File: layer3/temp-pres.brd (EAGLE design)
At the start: 16.5 x 12.7 mm, 9 parts, among them U1 TMP1021:1, U2 MS5803-14BA

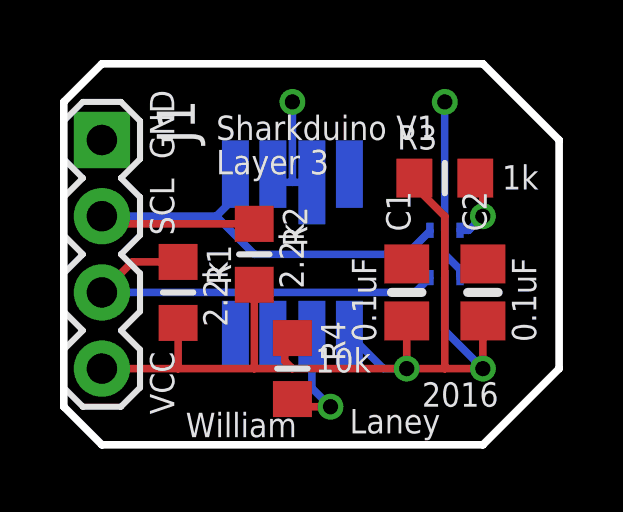
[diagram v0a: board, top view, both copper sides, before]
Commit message: silk screen
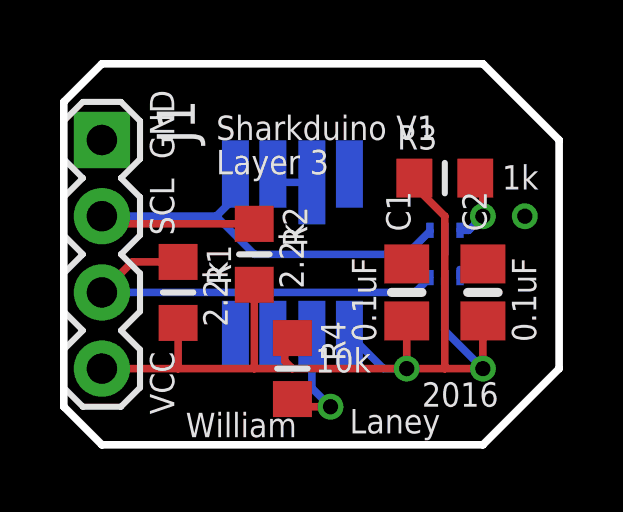
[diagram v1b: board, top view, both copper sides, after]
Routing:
- net GND: track 10.7 -> 3.00 mm, vias 2 -> 1
- added copper zone on layer 16, net GND
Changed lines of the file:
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@@
 <contactref element="C1" pad="2"/>
 <contactref element="C2" pad="2"/>
-<wire x1="8.27" y1="8.75" x2="7.62" y2="8.75" width="0.254" layer="16"/>
-<wire x1="7.62" y1="8.75" x2="7.245" y2="8.75" width="0.254" layer="16"/>
+<wire x1="8.27" y1="8.75" x2="7.245" y2="8.75" width="0.254" layer="16"/>
 <wire x1="7.245" y1="8.75" x2="6.97" y2="9.025" width="0.254" layer="16"/>
 <wire x1="8.27" y1="8.75" x2="8.27" y2="8.24" width="0.254" layer="16"/>
 <wire x1="13.205840625" y1="5.573584375" x2="13.205840625" y2="5.844159375" width="0.254" layer="16"/>
-<wire x1="13.205840625" y1="5.844159375" x2="12.7" y2="6.35" width="0.254" layer="16"/>
 <wire x1="12.7" y1="6.35" x2="12.7" y2="7.146696875" width="0.254" layer="16"/>
 <wire x1="12.7" y1="7.146696875" x2="12.696696875" y2="7.15" width="0.254" layer="16"/>
-<wire x1="12.696696875" y1="7.15" x2="12.696696875" y2="11.426696875" width="0.254" layer="16"/>
-<wire x1="12.696696875" y1="11.426696875" x2="12.7" y2="11.43" width="0.254" layer="16"/>
-<via x="12.7" y="11.43" extent="1-16" drill="0.508"/>
-<via x="7.62" y="11.43" extent="1-16" drill="0.508"/>
-<wire x1="7.62" y1="11.43" x2="7.62" y2="8.75" width="0.254" layer="16"/>
 <polygon width="0.254" layer="1" isolate="0.3048">
 <vertex x="0" y="11.43"/>
@@
 <vertex x="1.27" y="12.7"/>
 </polygon>
+<polygon width="0.254" layer="16" isolate="0.3048">
+<vertex x="1.524" y="12.7"/>
+<vertex x="13.97" y="12.7"/>
+<vertex x="16.51" y="10.16"/>
+<vertex x="16.51" y="2.54"/>
+<vertex x="13.97" y="0"/>
+<vertex x="1.143" y="0"/>
+<vertex x="1.143" y="0.127"/>
+<vertex x="0" y="1.27"/>
+<vertex x="0" y="11.43"/>
+<vertex x="1.27" y="12.7"/>
+</polygon>
+<via x="15.367" y="7.62" extent="1-16" drill="0.508"/>
 </signal>
 <signal name="SCL">

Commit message: tweeaked resistor placement
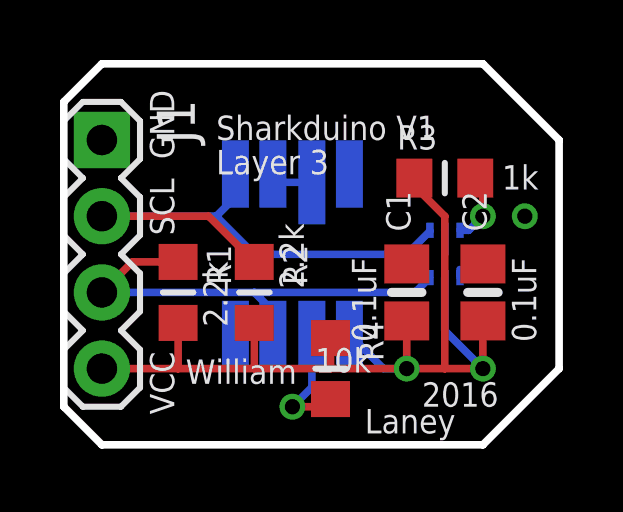
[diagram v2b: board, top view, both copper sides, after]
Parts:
- moved R4 1.27 mm to (8.89, 2.54)
- moved R2 1.27 mm to (6.35, 5.08)
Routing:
- net +3V3: track 34.6 -> 33.0 mm
- net SCL: track 18.7 -> 19.2 mm
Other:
- board text added: "MS5803-14BA"
- board text added: "SDA"
- board text added: "TMP102"
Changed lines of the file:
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@@
 <text x="5.08" y="10.16" size="0.8128" layer="21" font="vector" ratio="15">Sharkduino V1</text>
 <text x="5.08" y="9.017" size="0.8128" layer="21" font="vector" ratio="15">Layer 3</text>
-<text x="4.064" y="0.254" size="0.8128" layer="21" font="vector" ratio="15">William</text>
-<text x="9.525" y="0.381" size="0.8128" layer="21" font="vector" ratio="15">Laney</text>
+<text x="4.064" y="2.032" size="0.8128" layer="21" font="vector" ratio="15">William</text>
+<text x="10.033" y="0.381" size="0.8128" layer="21" font="vector" ratio="15">Laney</text>
 <text x="11.938" y="1.27" size="0.8128" layer="21" font="vector" ratio="15">2016</text>
+<text x="12.7" y="10.16" size="0.8128" layer="22" font="vector" ratio="15" rot="MR0">MS5803-14BA</text>
+<text x="11.049" y="5.207" size="0.8128" layer="22" font="vector" ratio="15" rot="MR180">TMP102</text>
+<text x="2.921" y="9.525" size="0.8128" layer="22" font="vector" ratio="15" rot="MR90">GND</text>
+<text x="2.921" y="6.604" size="0.8128" layer="22" font="vector" ratio="15" rot="MR90">SCL</text>
+<text x="2.921" y="1.27" size="0.8128" layer="22" font="vector" ratio="15" rot="MR90">VCC</text>
+<text x="2.921" y="4.064" size="0.8128" layer="22" font="vector" ratio="15" rot="MR90">SDA</text>
 </plain>
 <attributes>
@@
 </element>
 <element name="R1" library="microbuilder" package="_0805MP" value="2.2K" x="3.81" y="5.08" rot="R270"/>
-<element name="R2" library="microbuilder" package="_0805MP" value="2.2K" x="6.35" y="6.35" rot="R270"/>
+<element name="R2" library="microbuilder" package="_0805MP" value="2.2K" x="6.35" y="5.08" rot="R270"/>
 <element name="R3" library="microbuilder" package="_0805MP" value="1K" x="12.7" y="8.89"/>
-<element name="R4" library="microbuilder" package="_0805MP" value="10K" x="7.62" y="2.54" rot="R270"/>
+<element name="R4" library="microbuilder" package="_0805MP" value="10K" x="8.89" y="2.54" rot="R270"/>
 <element name="U1" library="SparkFun-Sensors" package="SOT563-2" value="TMP1021:1" x="12.7" y="6.35" rot="MR270"/>
 <element name="U2" library="MS5803" package="MS5803" value="MS5803-14BA" x="7.62" y="6.35" rot="MR270">
@@
 <wire x1="5.72" y1="8.26" x2="5.08" y2="7.62" width="0.254" layer="16"/>
 <wire x1="5.08" y1="7.62" x2="1.27" y2="7.62" width="0.254" layer="16"/>
-<wire x1="6.35" y1="7.366" x2="1.524" y2="7.366" width="0.254" layer="1"/>
-<wire x1="1.524" y1="7.366" x2="1.27" y2="7.62" width="0.254" layer="1"/>
 <wire x1="12.20203125" y1="7.15" x2="12.20203125" y2="7.12203125" width="0.254" layer="16"/>
 <wire x1="12.20203125" y1="7.12203125" x2="11.43" y2="6.35" width="0.254" layer="16"/>
 <wire x1="11.43" y1="6.35" x2="6.35" y2="6.35" width="0.254" layer="16"/>
 <wire x1="6.35" y1="6.35" x2="5.08" y2="7.62" width="0.254" layer="16"/>
+<wire x1="1.27" y1="7.62" x2="4.826" y2="7.62" width="0.254" layer="1"/>
+<wire x1="4.826" y1="7.62" x2="6.35" y2="6.096" width="0.254" layer="1"/>
 </signal>
 <signal name="SDA">
@@
 <contactref element="U2" pad="6"/>
 <contactref element="R4" pad="2"/>
-<wire x1="8.27" y1="3.675" x2="8.27" y2="1.89" width="0.254" layer="16"/>
-<wire x1="8.27" y1="1.89" x2="8.89" y2="1.27" width="0.254" layer="16"/>
-<via x="8.89" y="1.27" extent="1-16" drill="0.508"/>
-<wire x1="8.89" y1="1.27" x2="7.874" y2="1.27" width="0.254" layer="1"/>
-<wire x1="7.874" y1="1.27" x2="7.62" y2="1.524" width="0.254" layer="1"/>
+<via x="7.62" y="1.27" extent="1-16" drill="0.508"/>
+<wire x1="8.27" y1="3.675" x2="8.27" y2="1.92" width="0.254" layer="16"/>
+<wire x1="8.27" y1="1.92" x2="7.62" y2="1.27" width="0.254" layer="16"/>
+<wire x1="7.62" y1="1.27" x2="8.636" y2="1.27" width="0.254" layer="1"/>
+<wire x1="8.636" y1="1.27" x2="8.89" y2="1.524" width="0.254" layer="1"/>
 </signal>
 <signal name="+3V3">
@@
 <wire x1="1.27" y1="2.54" x2="3.81" y2="2.54" width="0.254" layer="1"/>
 <wire x1="3.81" y1="2.54" x2="6.35" y2="2.54" width="0.254" layer="1"/>
-<wire x1="6.35" y1="2.54" x2="7.62" y2="2.54" width="0.254" layer="1"/>
-<wire x1="7.62" y1="2.54" x2="11.43" y2="2.54" width="0.254" layer="1"/>
+<wire x1="6.35" y1="2.54" x2="8.89" y2="2.54" width="0.254" layer="1"/>
+<wire x1="8.89" y1="2.54" x2="11.43" y2="2.54" width="0.254" layer="1"/>
 <wire x1="3.81" y1="4.064" x2="3.81" y2="2.54" width="0.254" layer="1"/>
-<wire x1="6.35" y1="5.334" x2="6.35" y2="2.54" width="0.254" layer="1"/>
+<wire x1="6.35" y1="4.064" x2="6.35" y2="2.54" width="0.254" layer="1"/>
 <wire x1="13.97" y1="4.13" x2="13.97" y2="2.54" width="0.254" layer="1"/>
 <wire x1="13.97" y1="2.54" x2="12.7" y2="2.54" width="0.254" layer="1"/>
@@
 <wire x1="12.696696875" y1="5.573584375" x2="12.696696875" y2="3.813303125" width="0.254" layer="16"/>
 <wire x1="12.696696875" y1="3.813303125" x2="13.97" y2="2.54" width="0.254" layer="16"/>
-<wire x1="7.62" y1="3.556" x2="7.366" y2="3.556" width="0.254" layer="1"/>
 <wire x1="11.684" y1="8.89" x2="11.43" y2="8.89" width="0.254" layer="1"/>
 <via x="11.43" y="2.54" extent="1-16" drill="0.508"/>
 <wire x1="11.43" y1="8.89" x2="12.7" y2="7.62" width="0.254" layer="1"/>
 <wire x1="12.7" y1="7.62" x2="12.7" y2="2.54" width="0.254" layer="1"/>
-<wire x1="7.366" y1="3.556" x2="7.366" y2="2.794" width="0.254" layer="1"/>
-<wire x1="7.366" y1="2.794" x2="7.62" y2="2.54" width="0.254" layer="1"/>
+<wire x1="8.89" y1="3.556" x2="8.89" y2="2.54" width="0.254" layer="1"/>
 </signal>
 <signal name="N$1">

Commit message: added clearnece between components and leads
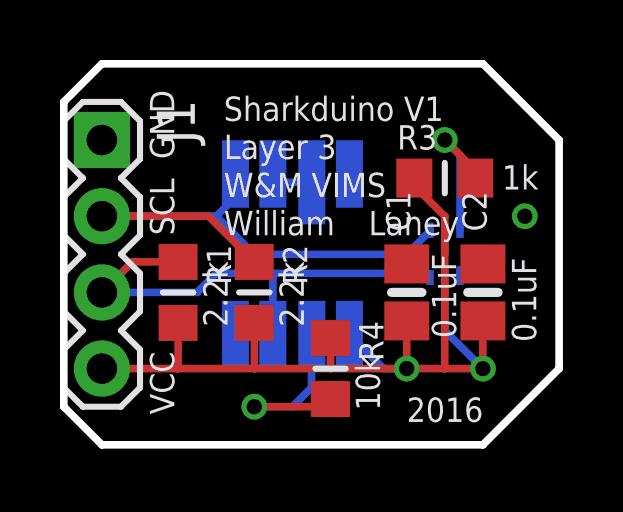
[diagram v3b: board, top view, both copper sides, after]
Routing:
- net N$1: track 2.33 -> 5.27 mm
- net PS: track 4.05 -> 6.59 mm
- net SDA: track 15.8 -> 16.3 mm
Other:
- board text added: "VIMS"
- board text added: "W&M"
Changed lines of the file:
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@@
 <setting verticaltext="up"/>
 </settings>
-<grid distance="0.005" unitdist="inch" unit="inch" style="lines" multiple="1" display="yes" altdistance="0.005" altunitdist="inch" altunit="inch"/>
+<grid distance="0.005" unitdist="inch" unit="inch" style="lines" multiple="1" display="yes" altdistance="0.025" altunitdist="inch" altunit="inch"/>
 <layers>
 <layer number="1" name="Top" color="4" fill="1" visible="yes" active="yes"/>
@@
 <text x="3.683" y="1.016" size="0.8128" layer="21" font="vector" ratio="15" rot="R90">VCC</text>
 <text x="15.748" y="3.429" size="0.8128" layer="21" font="vector" ratio="15" rot="R90">0.1uF</text>
-<text x="10.414" y="3.429" size="0.8128" layer="21" font="vector" ratio="15" rot="R90">0.1uF</text>
+<text x="13.081" y="3.556" size="0.8128" layer="21" font="vector" ratio="15" rot="R90">0.1uF</text>
 <text x="14.605" y="8.509" size="0.8128" layer="21" font="vector" ratio="15">1k</text>
-<text x="8.382" y="2.413" size="0.8128" layer="21" font="vector" ratio="15">10k</text>
+<text x="10.541" y="1.143" size="0.8128" layer="21" font="vector" ratio="15" rot="R90">10k</text>
 <text x="5.461" y="3.937" size="0.8128" layer="21" font="vector" ratio="15" rot="R90">2.2k</text>
-<text x="8.001" y="5.207" size="0.8128" layer="21" font="vector" ratio="15" rot="R90">2.2k</text>
-<text x="5.08" y="10.16" size="0.8128" layer="21" font="vector" ratio="15">Sharkduino V1</text>
-<text x="5.08" y="9.017" size="0.8128" layer="21" font="vector" ratio="15">Layer 3</text>
-<text x="4.064" y="2.032" size="0.8128" layer="21" font="vector" ratio="15">William</text>
-<text x="10.033" y="0.381" size="0.8128" layer="21" font="vector" ratio="15">Laney</text>
-<text x="11.938" y="1.27" size="0.8128" layer="21" font="vector" ratio="15">2016</text>
+<text x="8.001" y="3.937" size="0.8128" layer="21" font="vector" ratio="15" rot="R90">2.2k</text>
+<text x="5.334" y="10.795" size="0.8128" layer="21" font="vector" ratio="15">Sharkduino V1</text>
+<text x="5.334" y="9.525" size="0.8128" layer="21" font="vector" ratio="15">Layer 3</text>
+<text x="5.334" y="6.985" size="0.8128" layer="21" font="vector" ratio="15">William</text>
+<text x="10.16" y="6.985" size="0.8128" layer="21" font="vector" ratio="15">Laney</text>
+<text x="11.43" y="0.762" size="0.8128" layer="21" font="vector" ratio="15">2016</text>
 <text x="12.7" y="10.16" size="0.8128" layer="22" font="vector" ratio="15" rot="MR0">MS5803-14BA</text>
 <text x="11.049" y="5.207" size="0.8128" layer="22" font="vector" ratio="15" rot="MR180">TMP102</text>
@@
 <text x="2.921" y="1.27" size="0.8128" layer="22" font="vector" ratio="15" rot="MR90">VCC</text>
 <text x="2.921" y="4.064" size="0.8128" layer="22" font="vector" ratio="15" rot="MR90">SDA</text>
+<text x="5.334" y="8.255" size="0.8128" layer="21" font="vector" ratio="15">W&amp;M</text>
+<text x="8.255" y="8.255" size="0.8128" layer="21" font="vector" ratio="15">VIMS</text>
 </plain>
 <attributes>
@@
 <contactref element="R1" pad="1"/>
 <contactref element="U1" pad="6"/>
-<wire x1="6.97" y1="3.675" x2="6.97" y2="4.46" width="0.254" layer="16"/>
-<wire x1="6.97" y1="4.46" x2="6.35" y2="5.08" width="0.254" layer="16"/>
-<wire x1="6.35" y1="5.08" x2="1.27" y2="5.08" width="0.254" layer="16"/>
-<wire x1="6.35" y1="5.08" x2="11.708446875" y2="5.08" width="0.254" layer="16"/>
-<wire x1="11.708446875" y1="5.08" x2="12.20203125" y2="5.573584375" width="0.254" layer="16"/>
 <wire x1="3.81" y1="6.096" x2="2.286" y2="6.096" width="0.254" layer="1"/>
 <wire x1="2.286" y1="6.096" x2="1.27" y2="5.08" width="0.254" layer="1"/>
+<wire x1="1.27" y1="5.08" x2="4.445" y2="5.08" width="0.254" layer="16"/>
+<wire x1="4.445" y1="5.08" x2="5.08" y2="5.715" width="0.254" layer="16"/>
+<wire x1="5.08" y1="5.715" x2="6.985" y2="5.715" width="0.254" layer="16"/>
+<wire x1="6.985" y1="5.715" x2="12.060615625" y2="5.715" width="0.254" layer="16"/>
+<wire x1="12.060615625" y1="5.715" x2="12.20203125" y2="5.573584375" width="0.254" layer="16"/>
+<wire x1="6.97" y1="3.675" x2="6.97" y2="5.7" width="0.254" layer="16"/>
+<wire x1="6.97" y1="5.7" x2="6.985" y2="5.715" width="0.254" layer="16"/>
 </signal>
 <signal name="PS">
 <contactref element="U2" pad="6"/>
 <contactref element="R4" pad="2"/>
-<via x="7.62" y="1.27" extent="1-16" drill="0.508"/>
-<wire x1="8.27" y1="3.675" x2="8.27" y2="1.92" width="0.254" layer="16"/>
-<wire x1="8.27" y1="1.92" x2="7.62" y2="1.27" width="0.254" layer="16"/>
-<wire x1="7.62" y1="1.27" x2="8.636" y2="1.27" width="0.254" layer="1"/>
+<via x="6.35" y="1.27" extent="1-16" drill="0.508"/>
+<wire x1="6.35" y1="1.27" x2="8.636" y2="1.27" width="0.254" layer="1"/>
 <wire x1="8.636" y1="1.27" x2="8.89" y2="1.524" width="0.254" layer="1"/>
+<wire x1="6.35" y1="1.27" x2="7.62" y2="1.27" width="0.254" layer="16"/>
+<wire x1="7.62" y1="1.27" x2="8.255" y2="1.905" width="0.254" layer="16"/>
+<wire x1="8.255" y1="1.905" x2="8.255" y2="3.66" width="0.254" layer="16"/>
+<wire x1="8.255" y1="3.66" x2="8.27" y2="3.675" width="0.254" layer="16"/>
 </signal>
 <signal name="+3V3">
@@
 <contactref element="U1" pad="3"/>
 <contactref element="R3" pad="2"/>
-<wire x1="13.205840625" y1="7.15" x2="13.5" y2="7.15" width="0.254" layer="16"/>
-<wire x1="13.5" y1="7.15" x2="13.97" y2="7.62" width="0.254" layer="16"/>
-<via x="13.97" y="7.62" extent="1-16" drill="0.508"/>
-<wire x1="13.97" y1="7.62" x2="13.97" y2="8.636" width="0.254" layer="1"/>
+<via x="12.7" y="10.16" extent="1-16" drill="0.508"/>
 <wire x1="13.97" y1="8.636" x2="13.716" y2="8.89" width="0.254" layer="1"/>
+<wire x1="13.716" y1="8.89" x2="13.716" y2="9.144" width="0.254" layer="1"/>
+<wire x1="13.716" y1="9.144" x2="12.7" y2="10.16" width="0.254" layer="1"/>
+<wire x1="13.205840625" y1="7.15" x2="13.205840625" y2="9.654159375" width="0.254" layer="16"/>
+<wire x1="13.205840625" y1="9.654159375" x2="12.7" y2="10.16" width="0.254" layer="16"/>
 </signal>
 <signal name="N$3">
